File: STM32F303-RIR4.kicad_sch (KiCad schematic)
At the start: 34 parts, among them J0 CN7, J1 CN10, J101 LCC, J102 LCC, J103 S4 S3 S2 S1 SC, J104 MA MB NA NB, J105 - 12V +, J106 Servo 4, J107 Servo 3, J108 Servo 2, J109 Servo 1, J110 B1 C B2, U101 SN65HVD1050, U102 LM358, U103 TBD62064AFG, U104 TC4428, U105 TC4428, U106 G3VM-61VY4, U107 G3VM-61VY4

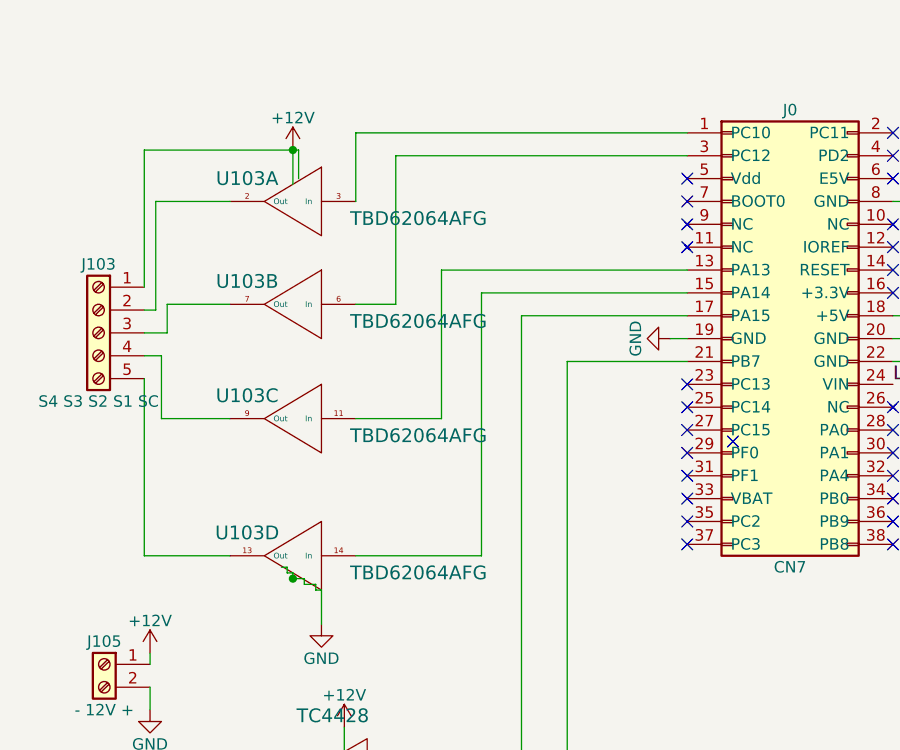
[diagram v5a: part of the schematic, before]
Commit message: Change Signal I/O pins.
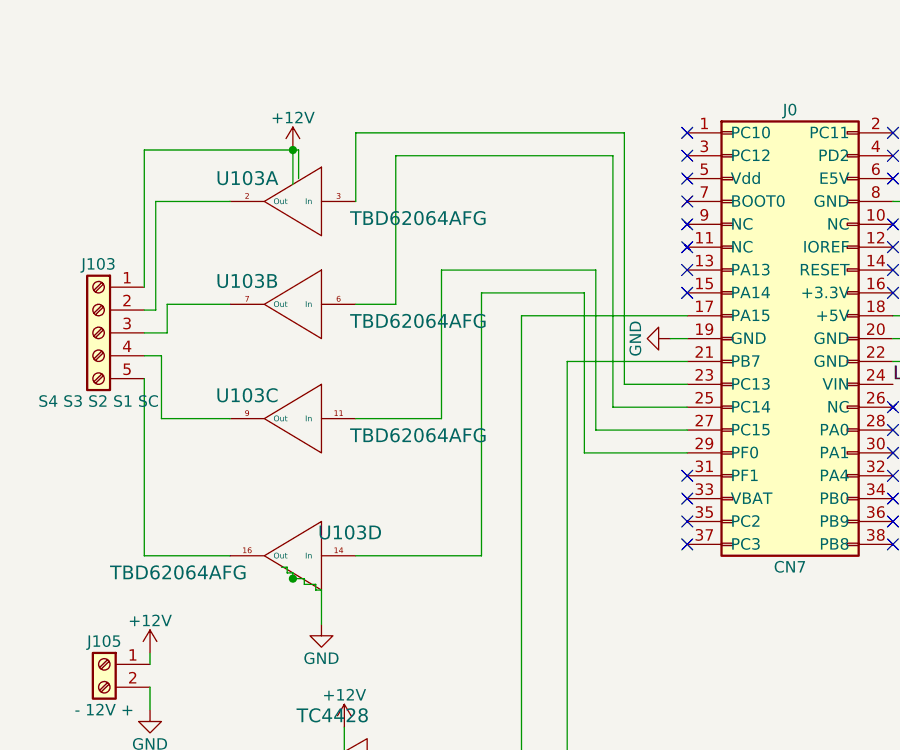
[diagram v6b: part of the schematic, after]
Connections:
- net at J0.1 (PC10): no longer U103.3 (In)
- net at J0.13 (PA13): no longer U103.11 (In)
- net at J0.15 (PA14): no longer U103.14 (In)
- net at J0.23 (PC13): now also U103.3 (In)
- net at J0.25 (PC14): now also U103.6 (In)
- net at J0.27 (PC15): now also U103.11 (In)
- net at J0.29 (PF0): now also U103.14 (In)
- net at J0.3 (PC12): no longer U103.6 (In)
- net at J103.5 (Pin_5): now also U103.16 (Out); no longer U103.13 (Out)
- no-connect marks 56 -> 55
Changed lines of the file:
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@@
   (no_connect (at 147.955 66.04))
   (no_connect (at 147.955 63.5))
-  (no_connect (at 84.455 64.77))
-  (no_connect (at 84.455 62.23))
   (no_connect (at 170.815 60.96))
   (no_connect (at 170.815 40.64))
-  (no_connect (at 84.455 59.69))
   (no_connect (at 147.955 53.34))
   (no_connect (at 147.955 76.2))
   (no_connect (at 184.15 132.715))
+  (no_connect (at 84.455 46.99))
   (no_connect (at 245.745 121.92))
   (no_connect (at 107.315 34.29))
-  (no_connect (at 89.535 66.04))
   (no_connect (at 147.955 68.58))
+  (no_connect (at 84.455 31.75))
   (no_connect (at 147.955 58.42))
   (no_connect (at 170.815 76.2))
@@
   (no_connect (at 170.815 43.18))
   (no_connect (at 107.315 69.85))
+  (no_connect (at 84.455 34.29))
   (no_connect (at 147.955 50.8))
   (no_connect (at 84.455 41.91))
@@
   (no_connect (at 170.815 78.74))
   (no_connect (at 170.815 50.8))
+  (no_connect (at 84.455 49.53))
   (no_connect (at 84.455 77.47))
   (no_connect (at 84.455 39.37))
@@
   (no_connect (at 147.955 60.96))
   (no_connect (at 107.315 49.53))
-  (no_connect (at 84.455 67.31))
   (no_connect (at 107.315 74.93))
   (no_connect (at 84.455 69.85))
@@
     (stroke (width 0) (type default) (color 0 0 0 0))
   )
-  (wire (pts (xy 57.15 46.99) (xy 84.455 46.99))
-    (stroke (width 0) (type default) (color 0 0 0 0))
-  )
   (wire (pts (xy 40.64 80.645) (xy 40.005 80.645))
     (stroke (width 0) (type default) (color 0 0 0 0))
@@
     (stroke (width 0) (type default) (color 0 0 0 0))
   )
-  (wire (pts (xy 52.07 34.29) (xy 84.455 34.29))
-    (stroke (width 0) (type default) (color 0 0 0 0))
-  )
   (wire (pts (xy 40.005 80.01) (xy 39.37 80.01))
     (stroke (width 0) (type default) (color 0 0 0 0))
@@
     (stroke (width 0) (type default) (color 0 0 0 0))
   )
+  (wire (pts (xy 77.47 31.75) (xy 47.625 31.75))
+    (stroke (width 0) (type default) (color 0 0 0 0))
+  )
   (wire (pts (xy 219.075 104.14) (xy 225.425 104.14))
     (stroke (width 0) (type default) (color 0 0 0 0))
@@
     (stroke (width 0) (type default) (color 0 0 0 0))
   )
+  (wire (pts (xy 84.455 62.23) (xy 76.2 62.23))
+    (stroke (width 0) (type default) (color 0 0 0 0))
+  )
   (wire (pts (xy 191.135 26.67) (xy 193.675 26.67))
     (stroke (width 0) (type default) (color 0 0 0 0))
@@
     (stroke (width 0) (type default) (color 0 0 0 0))
   )
+  (wire (pts (xy 74.295 46.99) (xy 57.15 46.99))
+    (stroke (width 0) (type default) (color 0 0 0 0))
+  )
   (wire (pts (xy 203.835 116.205) (xy 203.835 102.235))
     (stroke (width 0) (type default) (color 0 0 0 0))
@@
     (stroke (width 0) (type default) (color 0 0 0 0))
   )
+  (wire (pts (xy 76.2 62.23) (xy 76.2 34.29))
+    (stroke (width 0) (type default) (color 0 0 0 0))
+  )
   (wire (pts (xy 66.04 104.14) (xy 51.435 104.14))
     (stroke (width 0) (type default) (color 0 0 0 0))
@@
     (stroke (width 0) (type default) (color 0 0 0 0))
   )
+  (wire (pts (xy 84.455 64.77) (xy 74.295 64.77))
+    (stroke (width 0) (type default) (color 0 0 0 0))
+  )
   (wire (pts (xy 57.15 63.5) (xy 57.15 46.99))
     (stroke (width 0) (type default) (color 0 0 0 0))
@@
     (stroke (width 0) (type default) (color 0 0 0 0))
   )
+  (wire (pts (xy 84.455 59.69) (xy 77.47 59.69))
+    (stroke (width 0) (type default) (color 0 0 0 0))
+  )
+  (wire (pts (xy 73.025 67.31) (xy 73.025 49.53))
+    (stroke (width 0) (type default) (color 0 0 0 0))
+  )
   (wire (pts (xy 200.66 78.74) (xy 204.47 78.74))
     (stroke (width 0) (type default) (color 0 0 0 0))
@@
     (stroke (width 0) (type default) (color 0 0 0 0))
   )
-  (wire (pts (xy 61.595 49.53) (xy 84.455 49.53))
+  (wire (pts (xy 73.025 49.53) (xy 61.595 49.53))
     (stroke (width 0) (type default) (color 0 0 0 0))
   )
@@
     (stroke (width 0) (type default) (color 0 0 0 0))
   )
+  (wire (pts (xy 84.455 67.31) (xy 73.025 67.31))
+    (stroke (width 0) (type default) (color 0 0 0 0))
+  )
   (wire (pts (xy 22.86 136.525) (xy 29.21 136.525))
     (stroke (width 0) (type default) (color 0 0 0 0))
@@
     (stroke (width 0) (type default) (color 0 0 0 0))
   )
-  (wire (pts (xy 47.625 31.75) (xy 84.455 31.75))
-    (stroke (width 0) (type default) (color 0 0 0 0))
-  )
   (wire (pts (xy 192.405 33.655) (xy 196.85 33.655))
     (stroke (width 0) (type default) (color 0 0 0 0))
@@
     (stroke (width 0) (type default) (color 0 0 0 0))
   )
+  (wire (pts (xy 74.295 64.77) (xy 74.295 46.99))
+    (stroke (width 0) (type default) (color 0 0 0 0))
+  )
   (wire (pts (xy 43.815 86.36) (xy 43.815 82.55))
     (stroke (width 0) (type default) (color 0 0 0 0))
@@
     (stroke (width 0) (type default) (color 0 0 0 0))
   )
+  (wire (pts (xy 76.2 34.29) (xy 52.07 34.29))
+    (stroke (width 0) (type default) (color 0 0 0 0))
+  )
   (wire (pts (xy 66.04 52.07) (xy 66.04 104.14))
     (stroke (width 0) (type default) (color 0 0 0 0))
   )
   (wire (pts (xy 220.345 132.715) (xy 220.345 144.78))
+    (stroke (width 0) (type default) (color 0 0 0 0))
+  )
+  (wire (pts (xy 77.47 59.69) (xy 77.47 31.75))
     (stroke (width 0) (type default) (color 0 0 0 0))
   )
@@
     (pin "14")
   )
-  (symbol (lib_name "TBD62064AFG_1") (lib_id "tbd62064afg:TBD62064AFG") (at 41.275 78.74 0) (mirror y) (unit 4)
-    (in_bom yes) (on_board yes)
-    (property "Reference" "U103" (id 0) (at 35.56 76.2 0)
-      (effects (font (size 1.524 1.524)))
-    )
-    (property "Value" "TBD62064AFG" (id 1) (at 54.61 80.645 0)
-      (effects (font (size 1.524 1.524)))
-    )
-    (property "Footprint" "MyHSOP:HSOP16-P-300-1.00" (id 2) (at 46.355 71.755 0)
+  (symbol (lib_name "TBD62064AFG_2") (lib_id "tbd62064afg:TBD62064AFG") (at 41.275 78.74 0) (mirror y) (unit 4)
+    (in_bom yes) (on_board yes)
+    (property "Reference" "U103" (id 0) (at 46.99 76.2 0)
+      (effects (font (size 1.524 1.524)))
+    )
+    (property "Value" "TBD62064AFG" (id 1) (at 27.94 80.645 0)
+      (effects (font (size 1.524 1.524)))
+    )
+    (property "Footprint" "MyHSOP:HSOP16-P-300-1.00" (id 2) (at 36.195 71.755 0)
       (effects (font (size 1.524 1.524)) hide)
     )
@@
       (effects (font (size 1.524 1.524)))
     )
-    (property "Mouser Part Number" "757-TBD62064AFGEL " (id 4) (at 40.64 83.185 0)
+    (property "Mouser Part Number" "757-TBD62064AFGEL " (id 4) (at 41.91 83.185 0)
       (effects (font (size 1.27 1.27)) hide)
     )
@@
       (effects (font (size 1.27 1.27)) hide)
     )
-    (property "MPN" "TOSHIBA TBD62064AFG,EL" (id 6) (at 41.275 78.74 0)
+    (property "MPN" "TOSHIBA TBD62064AFG,EL" (id 6) (at 42.545 78.74 0)
       (effects (font (size 1.27 1.27)) hide)
     )
@@
     (pin "11")
     (pin "9")
-    (pin "13")
     (pin "14")
+    (pin "16")
   )
   (sheet_instances

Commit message: Correct Stall Motor driver part numbers.
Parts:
- U104, U105: LCSC C636863 -> C624948; MPN MICROCHIP TC1428COA -> Microchip TC4428ACOA713; Mouser Part Number 579-TC1428COA -> 579-TC4428ACOA713
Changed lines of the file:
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@@
       (effects (font (size 1.524 1.524)))
     )
-    (property "Mouser Part Number" "579-TC1428COA" (id 4) (at 45.085 104.14 0)
+    (property "Mouser Part Number" "579-TC4428ACOA713" (id 4) (at 45.085 104.14 0)
       (effects (font (size 1.27 1.27)) hide)
     )
-    (property "LCSC" "C636863" (id 5) (at 45.085 104.14 0)
+    (property "LCSC" "C624948" (id 5) (at 45.085 104.14 0)
       (effects (font (size 1.27 1.27)) hide)
     )
-    (property "MPN" "MICROCHIP TC1428COA" (id 6) (at 45.085 104.14 0)
+    (property "MPN" "Microchip TC4428ACOA713 " (id 6) (at 45.085 104.14 0)
       (effects (font (size 1.27 1.27)) hide)
     )
@@
       (effects (font (size 1.524 1.524)))
     )
-    (property "Mouser Part Number" "579-TC1428COA" (id 4) (at 45.085 125.73 0)
+    (property "Mouser Part Number" "579-TC4428ACOA713" (id 4) (at 45.085 125.73 0)
       (effects (font (size 1.27 1.27)) hide)
     )
-    (property "LCSC" "C636863" (id 5) (at 45.085 125.73 0)
+    (property "LCSC" "C624948" (id 5) (at 45.085 125.73 0)
       (effects (font (size 1.27 1.27)) hide)
     )
-    (property "MPN" "MICROCHIP TC1428COA" (id 6) (at 45.085 125.73 0)
+    (property "MPN" "Microchip TC4428ACOA713 " (id 6) (at 45.085 125.73 0)
       (effects (font (size 1.27 1.27)) hide)
     )
@@
       (effects (font (size 1.524 1.524)))
     )
-    (property "Mouser Part Number" "579-TC1428COA" (id 4) (at 44.45 144.78 0)
+    (property "Mouser Part Number" "579-TC4428ACOA713" (id 4) (at 44.45 144.78 0)
       (effects (font (size 1.27 1.27)) hide)
     )
-    (property "LCSC" "C636863" (id 5) (at 44.45 144.78 0)
+    (property "LCSC" "C624948" (id 5) (at 44.45 144.78 0)
       (effects (font (size 1.27 1.27)) hide)
     )
-    (property "MPN" "MICROCHIP TC1428COA" (id 6) (at 44.45 144.78 0)
+    (property "MPN" "Microchip TC4428ACOA713 " (id 6) (at 44.45 144.78 0)
       (effects (font (size 1.27 1.27)) hide)
     )
@@
       (effects (font (size 1.524 1.524)))
     )
-    (property "Mouser Part Number" "579-TC1428COA" (id 4) (at 44.45 167.005 0)
+    (property "Mouser Part Number" "579-TC4428ACOA713" (id 4) (at 44.45 167.005 0)
       (effects (font (size 1.27 1.27)) hide)
     )
-    (property "LCSC" "C636863" (id 5) (at 44.45 167.005 0)
+    (property "LCSC" "C624948" (id 5) (at 44.45 167.005 0)
       (effects (font (size 1.27 1.27)) hide)
     )
-    (property "MPN" "MICROCHIP TC1428COA" (id 6) (at 44.45 167.005 0)
+    (property "MPN" "Microchip TC4428ACOA713 " (id 6) (at 44.45 167.005 0)
       (effects (font (size 1.27 1.27)) hide)
     )

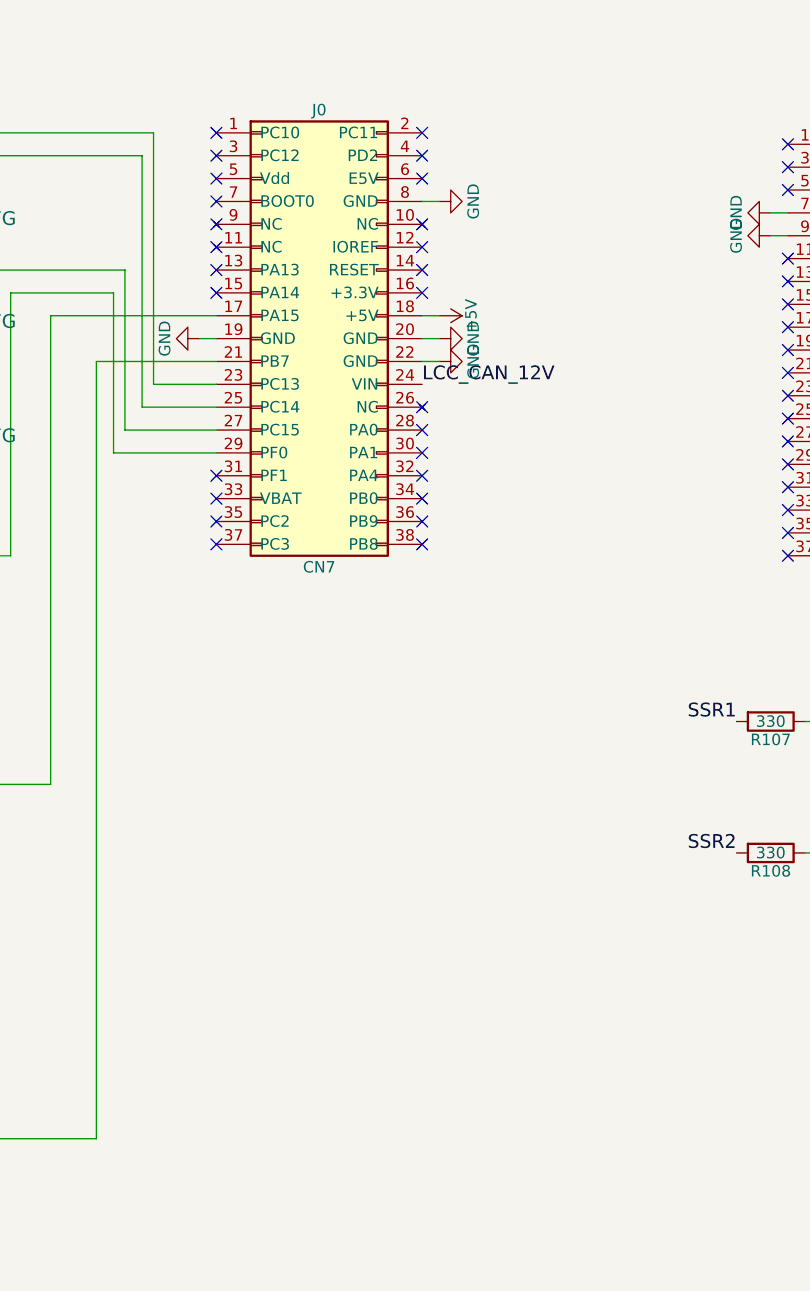
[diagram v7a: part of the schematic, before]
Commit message: Working on 5V power supply.
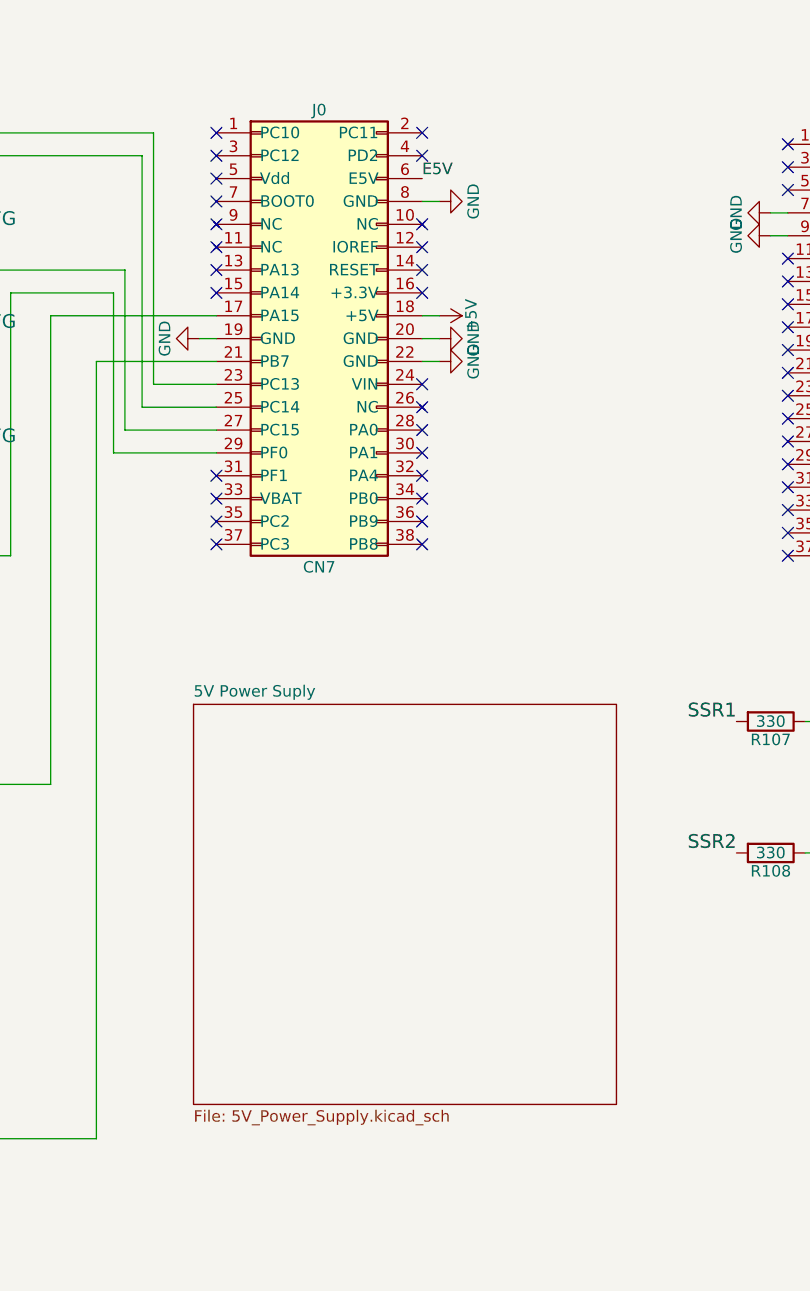
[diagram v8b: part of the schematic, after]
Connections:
- net LCC_CAN_12V: no longer J0.24 (VIN)
- net E5V: now reaches J0.6 (E5V)
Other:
- added sheet 5V Power Suply (5V_Power_Supply.kicad_sch)
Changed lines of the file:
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@@
   (no_connect (at 147.955 68.58))
   (no_connect (at 84.455 31.75))
+  (no_connect (at 107.315 59.69))
   (no_connect (at 147.955 58.42))
   (no_connect (at 170.815 76.2))
@@
   (no_connect (at 107.315 62.23))
   (no_connect (at 107.315 67.31))
-  (no_connect (at 107.315 36.83))
   (no_connect (at 147.955 38.1))
   (no_connect (at 147.955 60.96))
@@
     (effects (font (size 1.524 1.524)) (justify left bottom))
   )
+  (label "E5V" (at 107.315 36.83 0)
+    (effects (font (size 1.27 1.27)) (justify left bottom))
+  )
   (label "SSR2" (at 170.815 66.04 0)
     (effects (font (size 1.524 1.524)) (justify left bottom))
@@
   )
   (label "CAN_TX" (at 170.815 45.72 0)
-    (effects (font (size 1.524 1.524)) (justify left bottom))
-  )
-  (label "LCC_CAN_12V" (at 107.315 59.69 0)
     (effects (font (size 1.524 1.524)) (justify left bottom))
   )
@@
     (pin "16")
   )
+  (sheet (at 81.915 95.25) (size 46.99 44.45) (fields_autoplaced)
+    (stroke (width 0.1524) (type solid) (color 0 0 0 0))
+    (fill (color 0 0 0 0.0000))
+    (property "Sheet name" "5V Power Suply" (id 0) (at 81.915 94.5384 0)
+      (effects (font (size 1.27 1.27)) (justify left bottom))
+    )
+    (property "Sheet file" "5V_Power_Supply.kicad_sch" (id 1) (at 81.915 140.2846 0)
+      (effects (font (size 1.27 1.27)) (justify left top))
+    )
+  )
   (sheet_instances
     (path "/" (page "1"))
+    (path "/a1eed654-048f-4954-87cf-ae733d8334dc" (page "2"))
   )
   (symbol_instances
@@
       (reference "#PWR029") (unit 1) (value "GND") (footprint "")
     )
+    (path "/a1eed654-048f-4954-87cf-ae733d8334dc/56845fec-bf70-4243-9bcd-8767275d7958"
+      (reference "#PWR?") (unit 1) (value "GND") (footprint "")
+    )
     (path "/00000000-0000-0000-0000-0000642b2d14"
       (reference "C101") (unit 1) (value ".1 uf") (footprint "Capacitors_SMD:C_0603")
@@
       (reference "U107") (unit 1) (value "G3VM-61VY4") (footprint "Housings_SOIC:SO-4_4.4x4.3mm_Pitch2.54mm")
     )
-  )
+    (path "/a1eed654-048f-4954-87cf-ae733d8334dc/0152b6c9-1845-4945-a0c9-cd5369d0ec4c"
+      (reference "U?") (unit 1) (value "AP1509-50") (footprint "Package_SO:SOIC-8_3.9x4.9mm_P1.27mm")
+    )
+  )
